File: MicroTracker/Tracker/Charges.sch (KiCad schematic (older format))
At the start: 0 parts

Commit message: added connections
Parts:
- added J? (x2): Screw_Terminal_01x02, symbol Connector:Screw_Terminal_01x02
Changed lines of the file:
@@
 Comment4 ""
 $EndDescr
+$Comp
+L Connector:Screw_Terminal_01x02 J?
+U 1 1 5F0A9A98
+P 5750 4750
+F 0 "J?" V 5622 4830 50  0000 L CNN
+F 1 "Screw_Terminal_01x02" V 5713 4830 50  0000 L CNN
+F 2 "" H 5750 4750 50  0001 C CNN
+F 3 "~" H 5750 4750 50  0001 C CNN
+	1    5750 4750
+	0    1    1    0
+$EndComp
+$Comp
+L Connector:Screw_Terminal_01x02 J?
+U 1 1 5F0CF4AE
+P 4200 4750
+F 0 "J?" V 4072 4830 50  0000 L CNN
+F 1 "Screw_Terminal_01x02" V 4163 4830 50  0000 L CNN
+F 2 "" H 4200 4750 50  0001 C CNN
+F 3 "~" H 4200 4750 50  0001 C CNN
+	1    4200 4750
+	0    1    1    0
+$EndComp
 $EndSCHEMATC

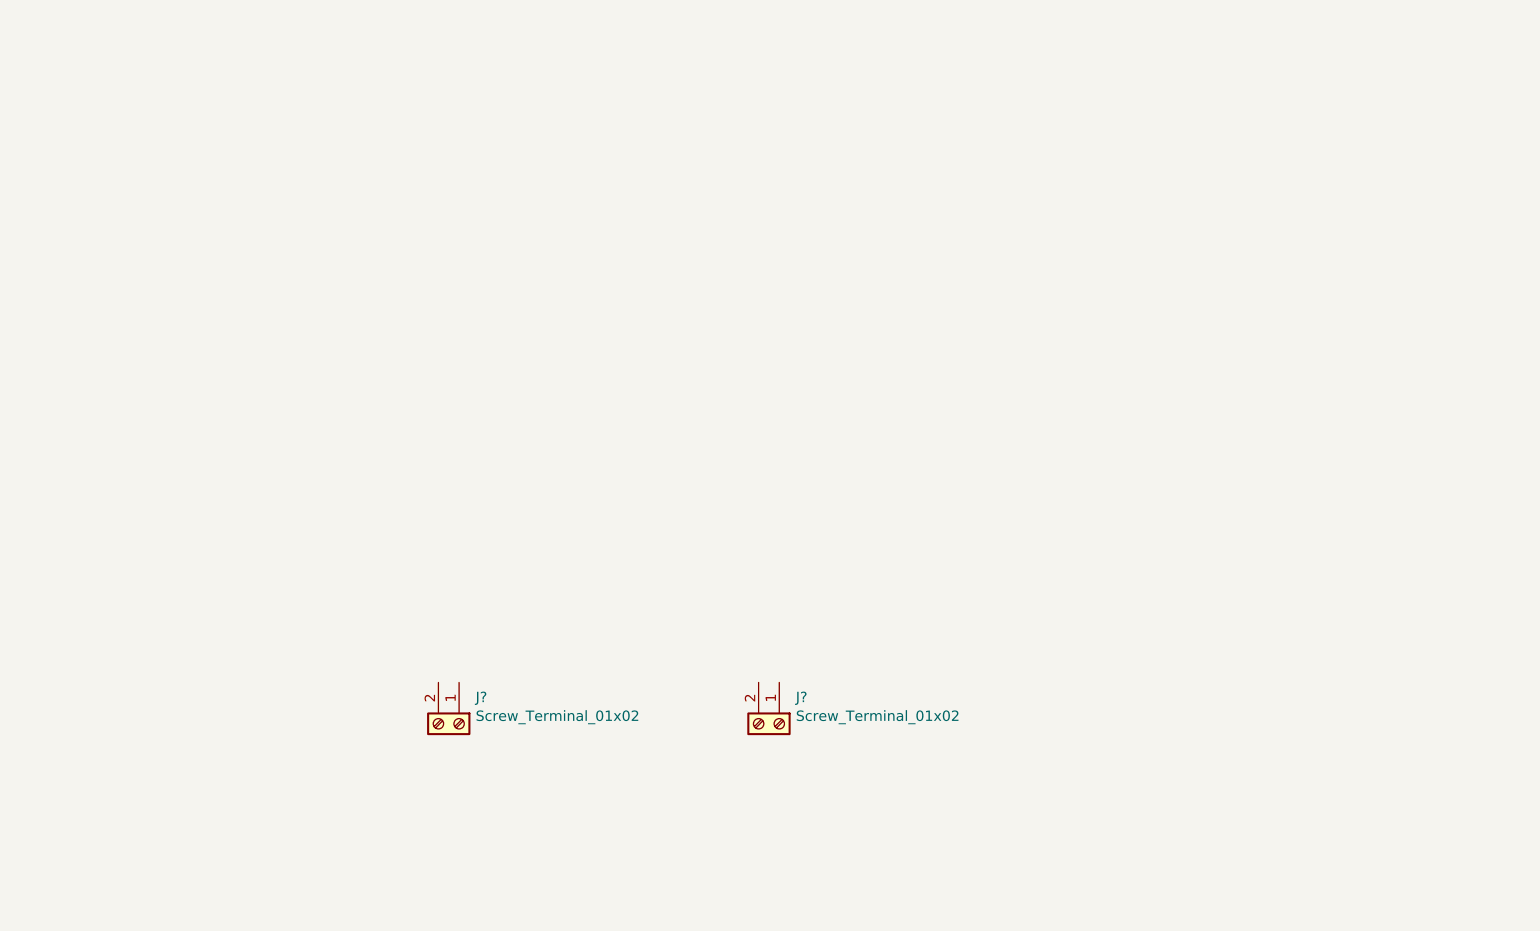
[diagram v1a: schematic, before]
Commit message: added charges
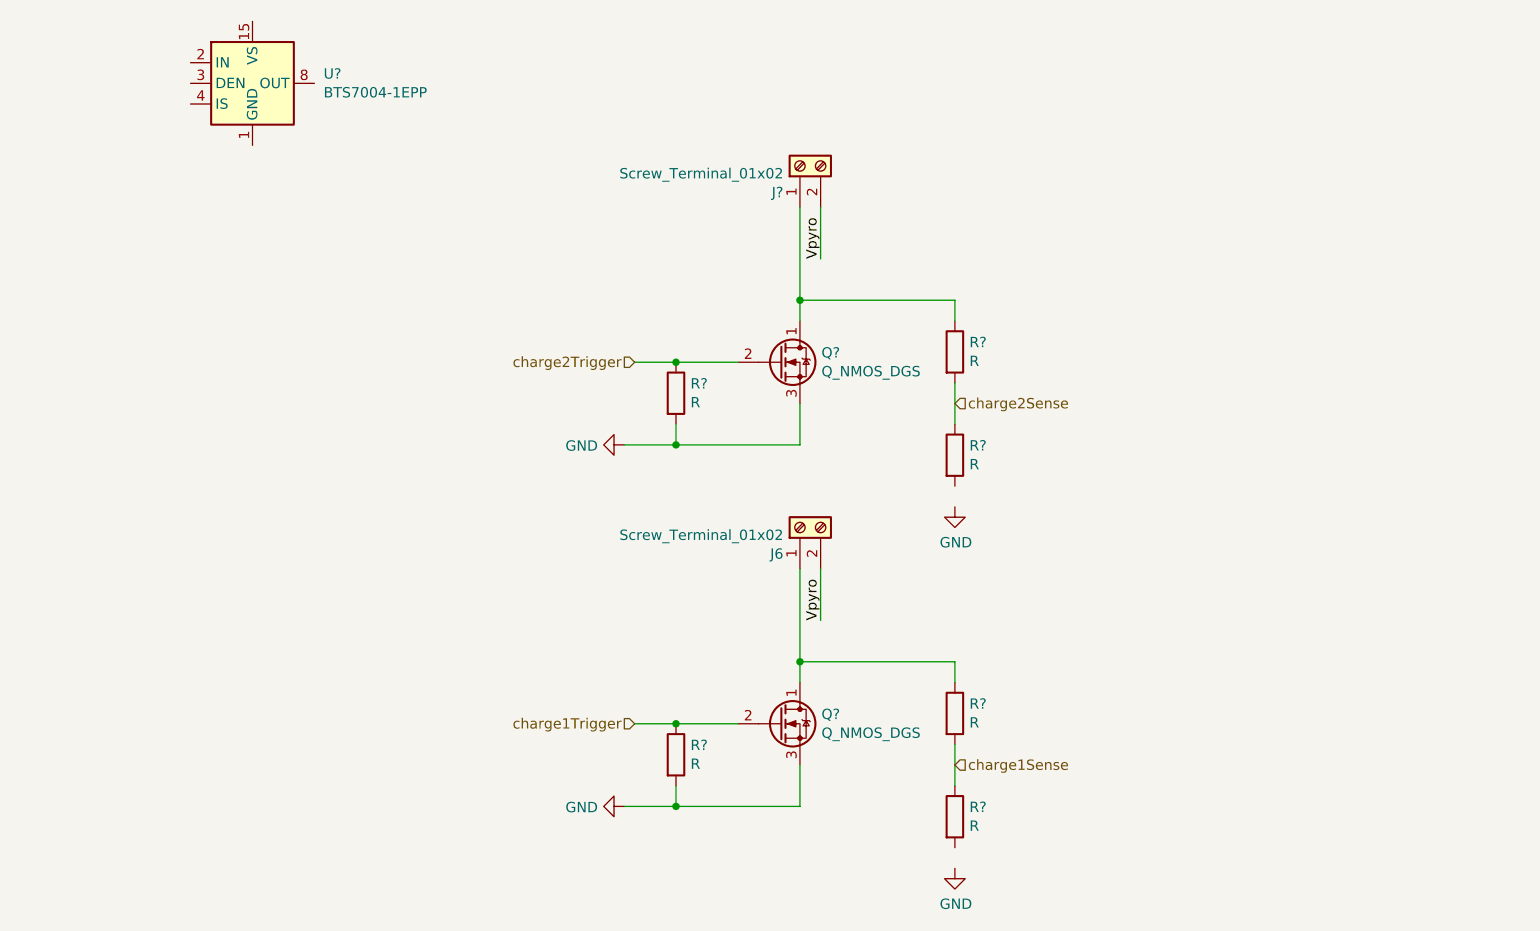
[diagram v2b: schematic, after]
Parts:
- removed J?: Screw_Terminal_01x02, symbol Connector:Screw_Terminal_01x02
- added J?: Screw_Terminal_01x02, symbol Connector:Screw_Terminal_01x02
- added Q? (x2): Q_NMOS_DGS, symbol Device:Q_NMOS_DGS
- added R? (x6): R, symbol Device:R
- added U?: BTS7004-1EPP, Package_SO:Infineon_PG-TSDSO-14-22, symbol Power_Management:BTS7004-1EPP
- gave numbers to parts that had none: 1
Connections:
- net at J6.1 (Pin_1): now also Q?.1 (D), R?.1
- net Vpyro: now reaches J6.2 (Pin_2)
- net Vpyro: now also J?.2 (Pin_2)
- new net: U?.10 (OUT), U?.12 (OUT), U?.13 (OUT), U?.14 (OUT), U?.8 (OUT), U?.9 (OUT)
- new net: J?.1 (Pin_1), Q?.1 (D), R?.1
- new net GND: Q?.3 (S), Q?.3 (S), R?.2, R?.2
- new net charge1Sense: R?.1, R?.2
- new net charge1Trigger: Q?.2 (G), R?.1
- new net charge2Sense: R?.1, R?.2
- new net charge2Trigger: Q?.2 (G), R?.1
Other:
- moved on the sheet: J6
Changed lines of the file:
@@
 $EndDescr
 $Comp
-L Connector:Screw_Terminal_01x02 J?
-U 1 1 5F0A9A98
+L Connector:Screw_Terminal_01x02 J6
+U 1 1 5F0CF4AE
+P 5850 3800
+F 0 "J6" V 5722 3880 50  0000 L CNN
+F 1 "Screw_Terminal_01x02" V 5813 3880 50  0000 L CNN
+F 2 "" H 5850 3800 50  0001 C CNN
+F 3 "~" H 5850 3800 50  0001 C CNN
+	1    5850 3800
+	0    -1   -1   0
+$EndComp
+Text HLabel 5050 4750 0    50   Input ~ 0
+charge1Trigger
+Text HLabel 5050 3000 0    50   Input ~ 0
+charge2Trigger
+Text HLabel 6600 3200 2    50   Input ~ 0
+charge2Sense
+Text HLabel 6600 4950 2    50   Input ~ 0
+charge1Sense
+$Comp
+L Power_Management:BTS7004-1EPP U?
+U 1 1 5F0FC048
+P 3200 1650
+F 0 "U?" H 3544 1696 50  0000 L CNN
+F 1 "BTS7004-1EPP" H 3544 1605 50  0000 L CNN
+F 2 "Package_SO:Infineon_PG-TSDSO-14-22" H 2300 1400 50  0001 C CNN
+F 3 "https://www.infineon.com/dgdl/Infineon-BTS7004-1EPP-DS-v01_00-EN.pdf?fileId=5546d4626102d35a016147550a725555" H 3200 1150 50  0001 C CNN
+	1    3200 1650
+	1    0    0    -1
+$EndComp
+$Comp
+L Device:R R?
+U 1 1 5F0FCAA9
+P 5250 4900
+F 0 "R?" H 5320 4946 50  0000 L CNN
+F 1 "R" H 5320 4855 50  0000 L CNN
+F 2 "" V 5180 4900 50  0001 C CNN
+F 3 "~" H 5250 4900 50  0001 C CNN
+	1    5250 4900
+	1    0    0    -1
+$EndComp
+Wire Wire Line
+	5050 4750 5250 4750
+$Comp
+L power:GND #PWR?
+U 1 1 5F0FDA83
+P 5000 5150
+F 0 "#PWR?" H 5000 4900 50  0001 C CNN
+F 1 "GND" V 5005 5022 50  0000 R CNN
+F 2 "" H 5000 5150 50  0001 C CNN
+F 3 "" H 5000 5150 50  0001 C CNN
+	1    5000 5150
+	0    1    1    0
+$EndComp
+Wire Wire Line
+	5000 5150 5250 5150
+Wire Wire Line
+	5250 5150 5250 5050
+$Comp
+L Device:R R?
+U 1 1 5F0FE29F
+P 6600 4700
+F 0 "R?" H 6670 4746 50  0000 L CNN
+F 1 "R" H 6670 4655 50  0000 L CNN
+F 2 "" V 6530 4700 50  0001 C CNN
+F 3 "~" H 6600 4700 50  0001 C CNN
+	1    6600 4700
+	1    0    0    -1
+$EndComp
+$Comp
+L Device:R R?
+U 1 1 5F0FEAAE
+P 6600 5200
+F 0 "R?" H 6670 5246 50  0000 L CNN
+F 1 "R" H 6670 5155 50  0000 L CNN
+F 2 "" V 6530 5200 50  0001 C CNN
+F 3 "~" H 6600 5200 50  0001 C CNN
+	1    6600 5200
+	1    0    0    -1
+$EndComp
+Wire Wire Line
+	6600 4850 6600 5050
+$Comp
+L power:GND #PWR?
+U 1 1 5F10057E
+P 6600 5450
+F 0 "#PWR?" H 6600 5200 50  0001 C CNN
+F 1 "GND" H 6605 5277 50  0000 C CNN
+F 2 "" H 6600 5450 50  0001 C CNN
+F 3 "" H 6600 5450 50  0001 C CNN
+	1    6600 5450
+	1    0    0    -1
+$EndComp
+$Comp
+L Device:Q_NMOS_DGS Q?
+U 1 1 5F100B87
 P 5750 4750
-F 0 "J?" V 5622 4830 50  0000 L CNN
-F 1 "Screw_Terminal_01x02" V 5713 4830 50  0000 L CNN
-F 2 "" H 5750 4750 50  0001 C CNN
+F 0 "Q?" H 5954 4796 50  0000 L CNN
+F 1 "Q_NMOS_DGS" H 5954 4705 50  0000 L CNN
+F 2 "" H 5950 4850 50  0001 C CNN
 F 3 "~" H 5750 4750 50  0001 C CNN
 	1    5750 4750
+	1    0    0    -1
+$EndComp
+Wire Wire Line
+	5250 4750 5550 4750
+Connection ~ 5250 4750
+Wire Wire Line
+	6600 4550 6600 4450
+Wire Wire Line
+	6600 4450 5850 4450
+Wire Wire Line
+	5850 4450 5850 4550
+Wire Wire Line
+	5850 4450 5850 4000
+Connection ~ 5850 4450
+Text Label 5950 4250 1    50   ~ 0
+Vpyro
+Wire Wire Line
+	5950 4250 5950 4000
+Wire Wire Line
+	5850 4950 5850 5150
+Wire Wire Line
+	5850 5150 5250 5150
+Connection ~ 5250 5150
+$Comp
+L Connector:Screw_Terminal_01x02 J?
+U 1 1 5F116245
+P 5850 2050
+F 0 "J?" V 5722 2130 50  0000 L CNN
+F 1 "Screw_Terminal_01x02" V 5813 2130 50  0000 L CNN
+F 2 "" H 5850 2050 50  0001 C CNN
+F 3 "~" H 5850 2050 50  0001 C CNN
+	1    5850 2050
+	0    -1   -1   0
+$EndComp
+$Comp
+L Device:R R?
+U 1 1 5F11624D
+P 5250 3150
+F 0 "R?" H 5320 3196 50  0000 L CNN
+F 1 "R" H 5320 3105 50  0000 L CNN
+F 2 "" V 5180 3150 50  0001 C CNN
+F 3 "~" H 5250 3150 50  0001 C CNN
+	1    5250 3150
+	1    0    0    -1
+$EndComp
+Wire Wire Line
+	5050 3000 5250 3000
+$Comp
+L power:GND #PWR?
+U 1 1 5F116254
+P 5000 3400
+F 0 "#PWR?" H 5000 3150 50  0001 C CNN
+F 1 "GND" V 5005 3272 50  0000 R CNN
+F 2 "" H 5000 3400 50  0001 C CNN
+F 3 "" H 5000 3400 50  0001 C CNN
+	1    5000 3400
 	0    1    1    0
 $EndComp
-$Comp
-L Connector:Screw_Terminal_01x02 J?
-U 1 1 5F0CF4AE
-P 4200 4750
-F 0 "J?" V 4072 4830 50  0000 L CNN
-F 1 "Screw_Terminal_01x02" V 4163 4830 50  0000 L CNN
-F 2 "" H 4200 4750 50  0001 C CNN
-F 3 "~" H 4200 4750 50  0001 C CNN
-	1    4200 4750
-	0    1    1    0
-$EndComp
+Wire Wire Line
+	5000 3400 5250 3400
+Wire Wire Line
+	5250 3400 5250 3300
+$Comp
+L Device:R R?
+U 1 1 5F11625C
+P 6600 2950
+F 0 "R?" H 6670 2996 50  0000 L CNN
+F 1 "R" H 6670 2905 50  0000 L CNN
+F 2 "" V 6530 2950 50  0001 C CNN
+F 3 "~" H 6600 2950 50  0001 C CNN
+	1    6600 2950
+	1    0    0    -1
+$EndComp
+$Comp
+L Device:R R?
+U 1 1 5F116262
+P 6600 3450
+F 0 "R?" H 6670 3496 50  0000 L CNN
+F 1 "R" H 6670 3405 50  0000 L CNN
+F 2 "" V 6530 3450 50  0001 C CNN
+F 3 "~" H 6600 3450 50  0001 C CNN
+	1    6600 3450
+	1    0    0    -1
+$EndComp
+Wire Wire Line
+	6600 3100 6600 3300
+$Comp
+L power:GND #PWR?
+U 1 1 5F116269
+P 6600 3700
+F 0 "#PWR?" H 6600 3450 50  0001 C CNN
+F 1 "GND" H 6605 3527 50  0000 C CNN
+F 2 "" H 6600 3700 50  0001 C CNN
+F 3 "" H 6600 3700 50  0001 C CNN
+	1    6600 3700
+	1    0    0    -1
+$EndComp
+$Comp
+L Device:Q_NMOS_DGS Q?
+U 1 1 5F11626F
+P 5750 3000
+F 0 "Q?" H 5954 3046 50  0000 L CNN
+F 1 "Q_NMOS_DGS" H 5954 2955 50  0000 L CNN
+F 2 "" H 5950 3100 50  0001 C CNN
+F 3 "~" H 5750 3000 50  0001 C CNN
+	1    5750 3000
+	1    0    0    -1
+$EndComp
+Wire Wire Line
+	5250 3000 5550 3000
+Connection ~ 5250 3000
+Wire Wire Line
+	6600 2800 6600 2700
+Wire Wire Line
+	6600 2700 5850 2700
+Wire Wire Line
+	5850 2700 5850 2800
+Wire Wire Line
+	5850 2700 5850 2250
+Connection ~ 5850 2700
+Text Label 5950 2500 1    50   ~ 0
+Vpyro
+Wire Wire Line
+	5950 2500 5950 2250
+Wire Wire Line
+	5850 3200 5850 3400
+Wire Wire Line
+	5850 3400 5250 3400
+Connection ~ 5250 3400
 $EndSCHEMATC

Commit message: assigned parts
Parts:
- R21, R22, R23, R24, R25, R26: renamed from R?; footprint (none) -> Resistor_SMD:R_0805_2012Metric_Pad1.15x1.40mm_HandSolder
- gave numbers to parts that had none: 4
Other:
- moved on the sheet: J6, J7, Q2, Q3, R21, R22, R23, R24, R25, R26, U11

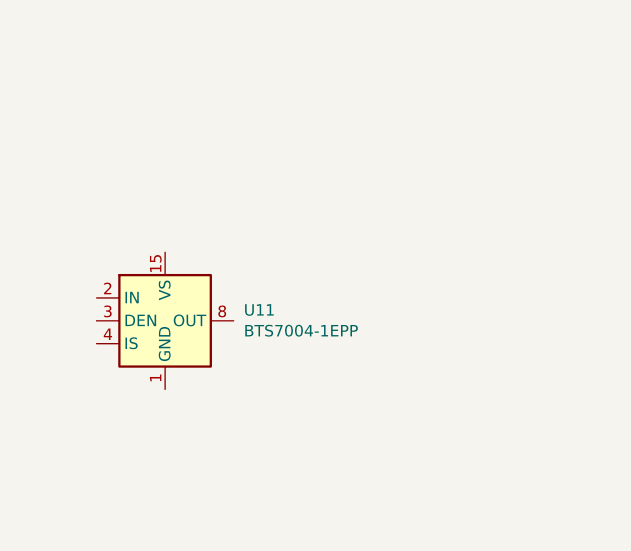
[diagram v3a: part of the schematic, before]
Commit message: added more parts and lib
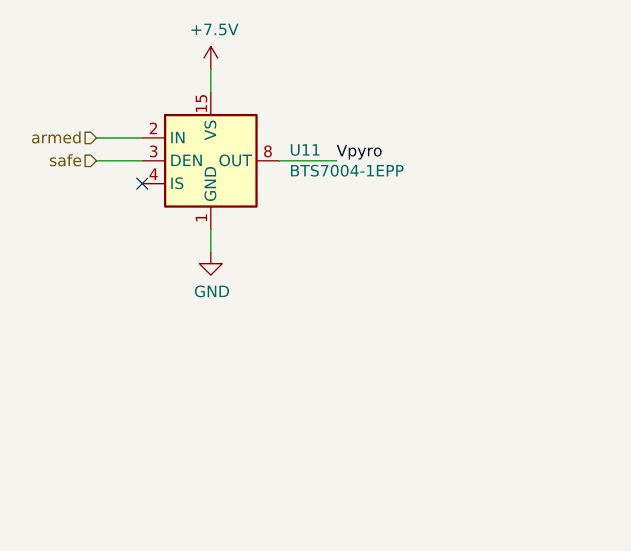
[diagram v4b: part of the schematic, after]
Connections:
- net GND: now also U11.1 (GND)
- net Vpyro: now also U11.10 (OUT), U11.12 (OUT), U11.13 (OUT), U11.14 (OUT), U11.8 (OUT), U11.9 (OUT)
- net +7.5V: now reaches U11.15 (VS)
- net armed: now reaches U11.2 (IN)
- net safe: now reaches U11.3 (DEN)
- no-connect marks 0 -> 1
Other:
- moved on the sheet: U11
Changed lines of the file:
@@
 L Power_Management:BTS7004-1EPP U11
 U 1 1 5F0FC048
-P 2700 2650
-F 0 "U11" H 3044 2696 50  0000 L CNN
-F 1 "BTS7004-1EPP" H 3044 2605 50  0000 L CNN
-F 2 "Package_SO:Infineon_PG-TSDSO-14-22" H 1800 2400 50  0001 C CNN
-F 3 "https://www.infineon.com/dgdl/Infineon-BTS7004-1EPP-DS-v01_00-EN.pdf?fileId=5546d4626102d35a016147550a725555" H 2700 2150 50  0001 C CNN
-	1    2700 2650
+P 2900 1950
+F 0 "U11" H 3244 1996 50  0000 L CNN
+F 1 "BTS7004-1EPP" H 3244 1905 50  0000 L CNN
+F 2 "Package_SO:Infineon_PG-TSDSO-14-22" H 2000 1700 50  0001 C CNN
+F 3 "https://www.infineon.com/dgdl/Infineon-BTS7004-1EPP-DS-v01_00-EN.pdf?fileId=5546d4626102d35a016147550a725555" H 2900 1450 50  0001 C CNN
+	1    2900 1950
 	1    0    0    -1
 $EndComp
@@
 	7950 3150 7350 3150
 Connection ~ 7350 3150
+$Comp
+L power:GND #PWR0113
+U 1 1 5F1CA43C
+P 2900 2350
+F 0 "#PWR0113" H 2900 2100 50  0001 C CNN
+F 1 "GND" H 2905 2177 50  0000 C CNN
+F 2 "" H 2900 2350 50  0001 C CNN
+F 3 "" H 2900 2350 50  0001 C CNN
+	1    2900 2350
+	1    0    0    -1
+$EndComp
+$Comp
+L power:+7.5V #PWR0114
+U 1 1 5F1CAA75
+P 2900 1550
+F 0 "#PWR0114" H 2900 1400 50  0001 C CNN
+F 1 "+7.5V" H 2915 1723 50  0000 C CNN
+F 2 "" H 2900 1550 50  0001 C CNN
+F 3 "" H 2900 1550 50  0001 C CNN
+	1    2900 1550
+	1    0    0    -1
+$EndComp
+Text Label 3450 1950 0    50   ~ 0
+Vpyro
+Text HLabel 2400 1850 0    50   Input ~ 0
+armed
+Text HLabel 2400 1950 0    50   Input ~ 0
+safe
+Wire Wire Line
+	2400 1850 2600 1850
+Wire Wire Line
+	2400 1950 2600 1950
+NoConn ~ 2600 2050
+Wire Wire Line
+	2900 2250 2900 2350
+Wire Wire Line
+	2900 1650 2900 1550
+Wire Wire Line
+	3200 1950 3450 1950
 $EndSCHEMATC

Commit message: fixed errors
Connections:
- net GND: now also R24.2, R26.2
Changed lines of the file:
@@
 Wire Wire Line
 	3200 1950 3450 1950
+Wire Wire Line
+	8700 3350 8700 3450
+Wire Wire Line
+	8700 5100 8700 5200
 $EndSCHEMATC
